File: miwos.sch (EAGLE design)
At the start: 44 parts

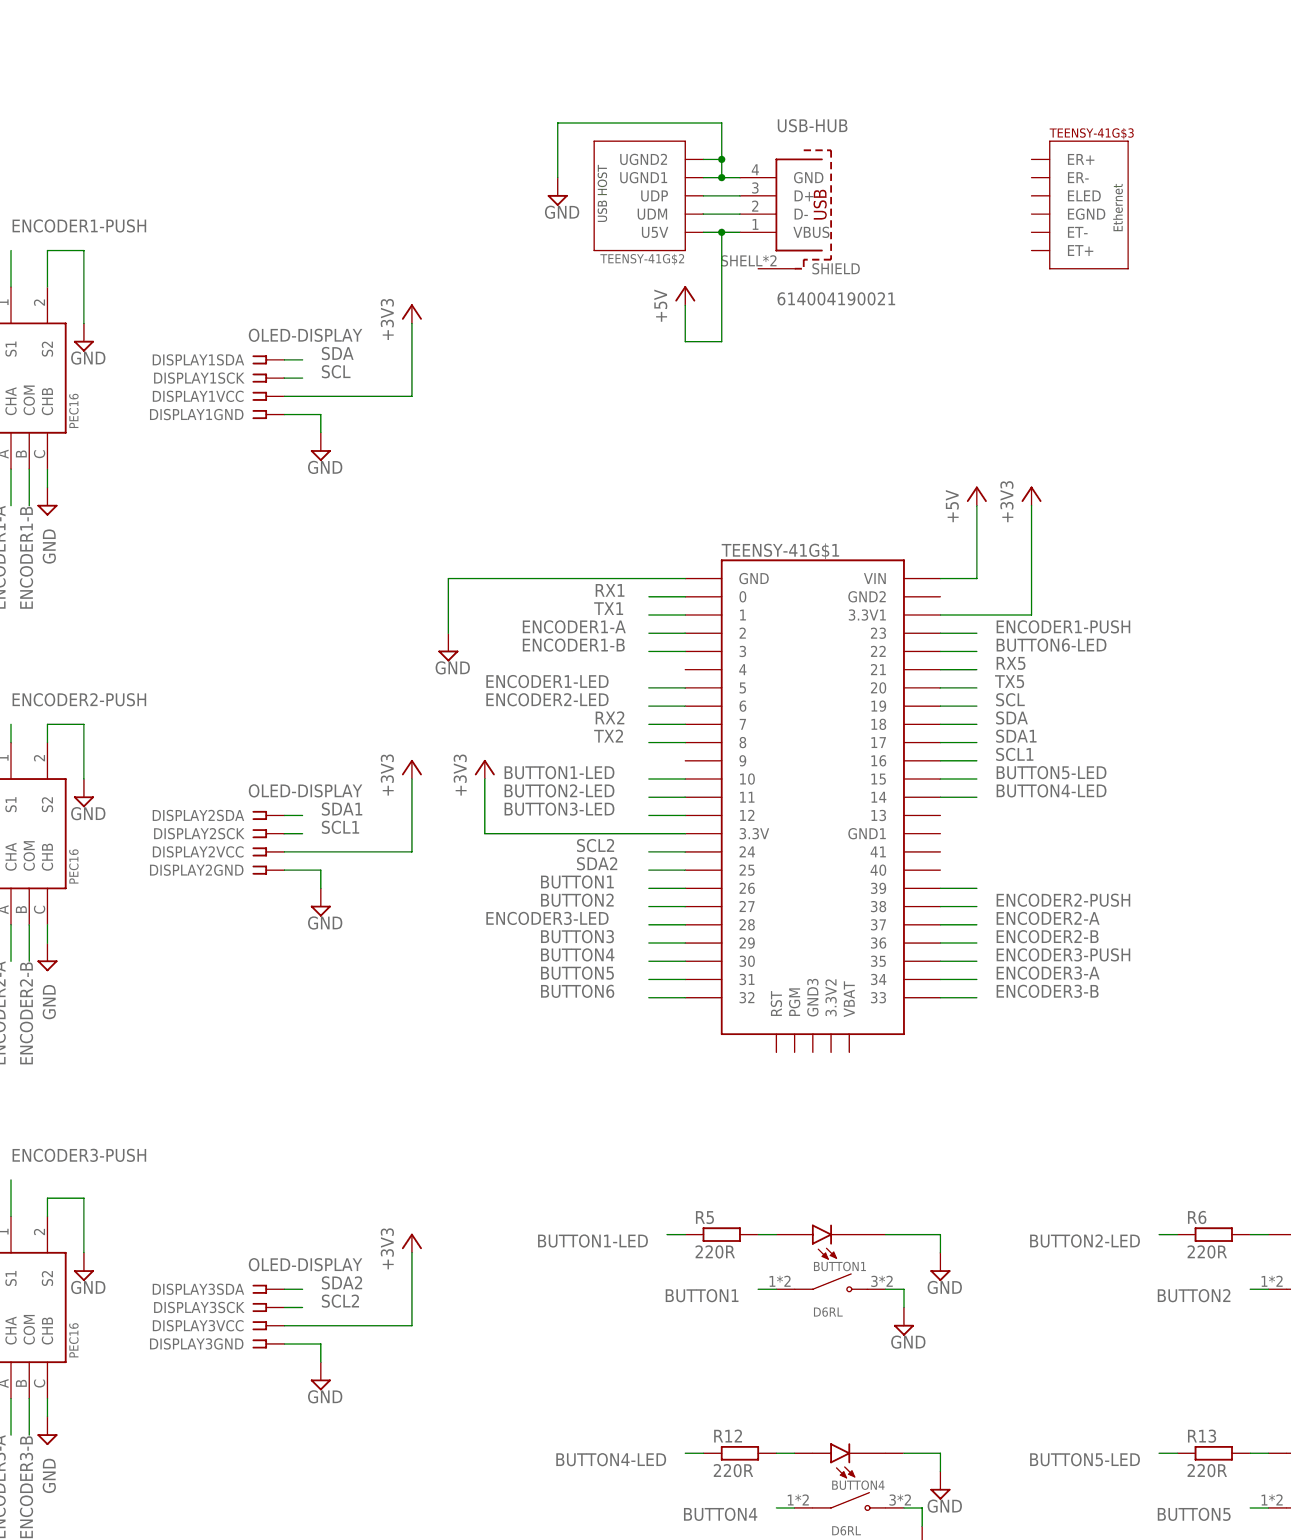
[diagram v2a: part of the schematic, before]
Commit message: Use DFR0647 displays
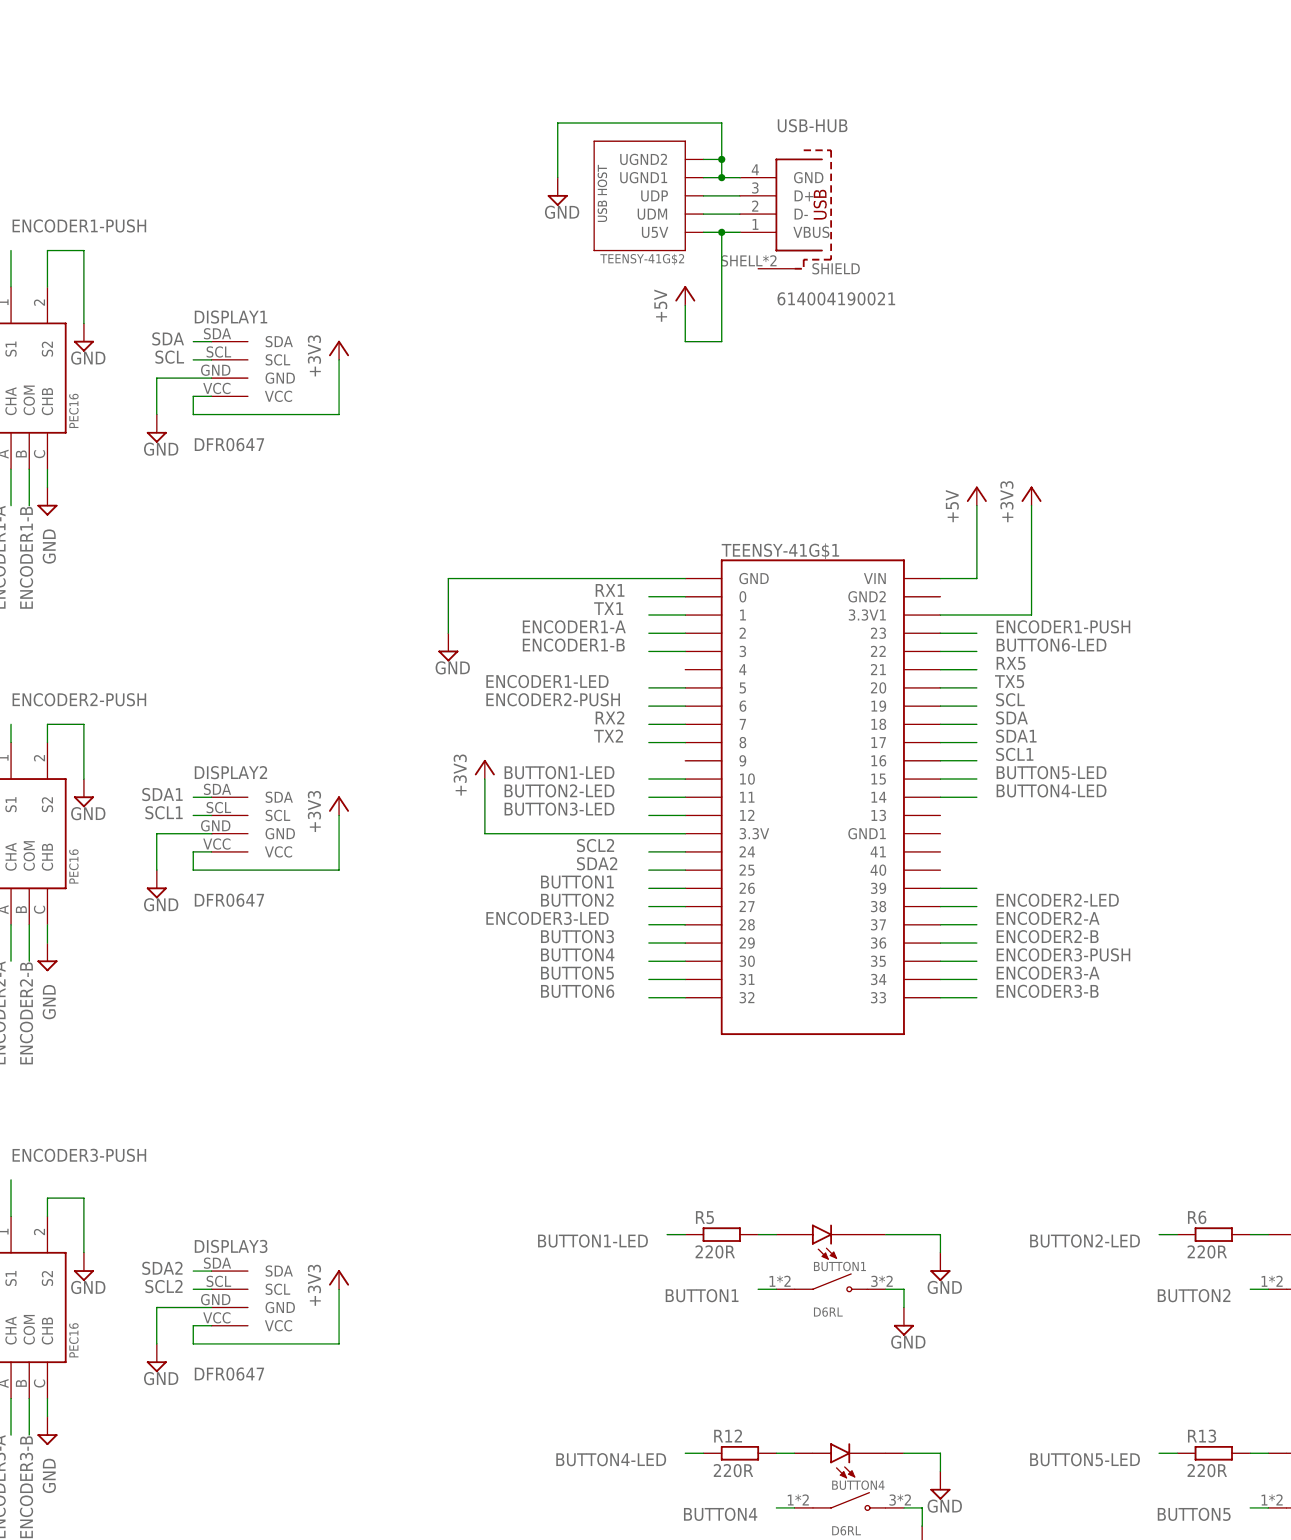
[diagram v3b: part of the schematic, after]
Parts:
- DISPLAY1, DISPLAY2, DISPLAY3: value OLED-DISPLAY -> DFR0647; device oled-display:OLED-DISPLAY -> DFR0647:DFR0647
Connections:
- net +3V3: now also DISPLAY1.VCC, DISPLAY2.VCC, DISPLAY3.VCC; no longer DISPLAY1VCC.1, DISPLAY2VCC.1, DISPLAY3VCC.1
- net ENCODER2-LED: now also TEENSY-41G$1.38; no longer TEENSY-41G$1.6
- net ENCODER2-PUSH: now also TEENSY-41G$1.6; no longer TEENSY-41G$1.38
- net GND: now also DISPLAY1.GND, DISPLAY2.GND, DISPLAY3.GND; no longer DISPLAY1GND.1, DISPLAY2GND.1, DISPLAY3GND.1
- net SCL: now also DISPLAY1.SCL; no longer DISPLAY1SCK.1
- net SCL1: now also DISPLAY2.SCL; no longer DISPLAY2SCK.1
- net SCL2: now also DISPLAY3.SCL; no longer DISPLAY3SCK.1
- net SDA: now also DISPLAY1.SDA; no longer DISPLAY1SDA.1
- net SDA1: now also DISPLAY2.SDA; no longer DISPLAY2SDA.1
- net SDA2: now also DISPLAY3.SDA; no longer DISPLAY3SDA.1

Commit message: Use 6N138 SMD footprint
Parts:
- OK1, OK2: device optocoupler:6N138 -> 6N138:6N138
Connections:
- net ENCODER1-B: now also ENCODER1.CHB; no longer ENCODER1.COM
- net ENCODER2-B: now also ENCODER2.CHB; no longer ENCODER2.COM
- net ENCODER3-B: now also ENCODER3.CHB; no longer ENCODER3.COM
- net GND: now also ENCODER1.COM, ENCODER2.COM, ENCODER3.COM; no longer ENCODER1.CHB, ENCODER2.CHB, ENCODER3.CHB
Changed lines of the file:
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@@
 <part name="SUPPLY5" library="supply2" library_urn="urn:adsk.eagle:library:372" deviceset="GND" device=""/>
 <part name="SUPPLY6" library="supply2" library_urn="urn:adsk.eagle:library:372" deviceset="GND" device=""/>
-<part name="OK1" library="optocoupler" library_urn="urn:adsk.eagle:library:320" deviceset="6N138" device="" package3d_urn="urn:adsk.eagle:package:21941/1"/>
+<part name="OK1" library="6N138" deviceset="6N138" device="" package3d_urn="urn:adsk.eagle:package:21941/1"/>
 <part name="MIDI2-IN" library="adafruit-5pin-din" deviceset="ADAFRUIT-5PIN-DIN" device=""/>
 <part name="SUPPLY7" library="supply2" library_urn="urn:adsk.eagle:library:372" deviceset="GND" device=""/>
@@
 <part name="SUPPLY19" library="supply2" library_urn="urn:adsk.eagle:library:372" deviceset="GND" device=""/>
 <part name="R7" library="rcl" library_urn="urn:adsk.eagle:library:334" deviceset="R-EU_" device="R0603" package3d_urn="urn:adsk.eagle:package:23555/3" value="220R"/>
-<part name="OK2" library="optocoupler" library_urn="urn:adsk.eagle:library:320" deviceset="6N138" device="" package3d_urn="urn:adsk.eagle:package:21941/1"/>
+<part name="OK2" library="6N138" deviceset="6N138" device="" package3d_urn="urn:adsk.eagle:package:21941/1"/>
 <part name="MIDI1-IN" library="adafruit-5pin-din" deviceset="ADAFRUIT-5PIN-DIN" device=""/>
 <part name="SUPPLY20" library="supply2" library_urn="urn:adsk.eagle:library:372" deviceset="GND" device=""/>
@@
 </segment>
 <segment>
-<pinref part="ENCODER1" gate="G$1" pin="CHB"/>
+<pinref part="ENCODER1" gate="G$1" pin="COM"/>
 <pinref part="SUPPLY1" gate="GND" pin="GND"/>
 <wire x1="-81.28" y1="104.14" x2="-81.28" y2="106.68" width="0.1524" layer="91"/>
 </segment>
 <segment>
-<pinref part="ENCODER2" gate="G$1" pin="CHB"/>
+<pinref part="ENCODER2" gate="G$1" pin="COM"/>
 <pinref part="SUPPLY3" gate="GND" pin="GND"/>
 <wire x1="-81.28" y1="43.18" x2="-81.28" y2="40.64" width="0.1524" layer="91"/>
 </segment>
 <segment>
-<pinref part="ENCODER3" gate="G$1" pin="CHB"/>
+<pinref part="ENCODER3" gate="G$1" pin="COM"/>
 <wire x1="-81.28" y1="-22.86" x2="-81.28" y2="-25.4" width="0.1524" layer="91"/>
 <pinref part="SUPPLY5" gate="GND" pin="GND"/>
@@
 </segment>
 <segment>
-<pinref part="ENCODER3" gate="G$1" pin="COM"/>
+<pinref part="ENCODER3" gate="G$1" pin="CHB"/>
 <wire x1="-83.82" y1="-22.86" x2="-83.82" y2="-27.94" width="0.1524" layer="91"/>
 <label x="-85.09" y="-27.94" size="1.778" layer="95" rot="R270"/>
@@
 </segment>
 <segment>
-<pinref part="ENCODER2" gate="G$1" pin="COM"/>
+<pinref part="ENCODER2" gate="G$1" pin="CHB"/>
 <wire x1="-83.82" y1="43.18" x2="-83.82" y2="38.1" width="0.1524" layer="91"/>
 <label x="-85.09" y="38.1" size="1.778" layer="95" rot="R270"/>
@@
 </segment>
 <segment>
-<pinref part="ENCODER1" gate="G$1" pin="COM"/>
+<pinref part="ENCODER1" gate="G$1" pin="CHB"/>
 <wire x1="-83.82" y1="106.68" x2="-83.82" y2="101.6" width="0.1524" layer="91"/>
 <label x="-85.09" y="101.6" size="1.778" layer="95" rot="R270"/>

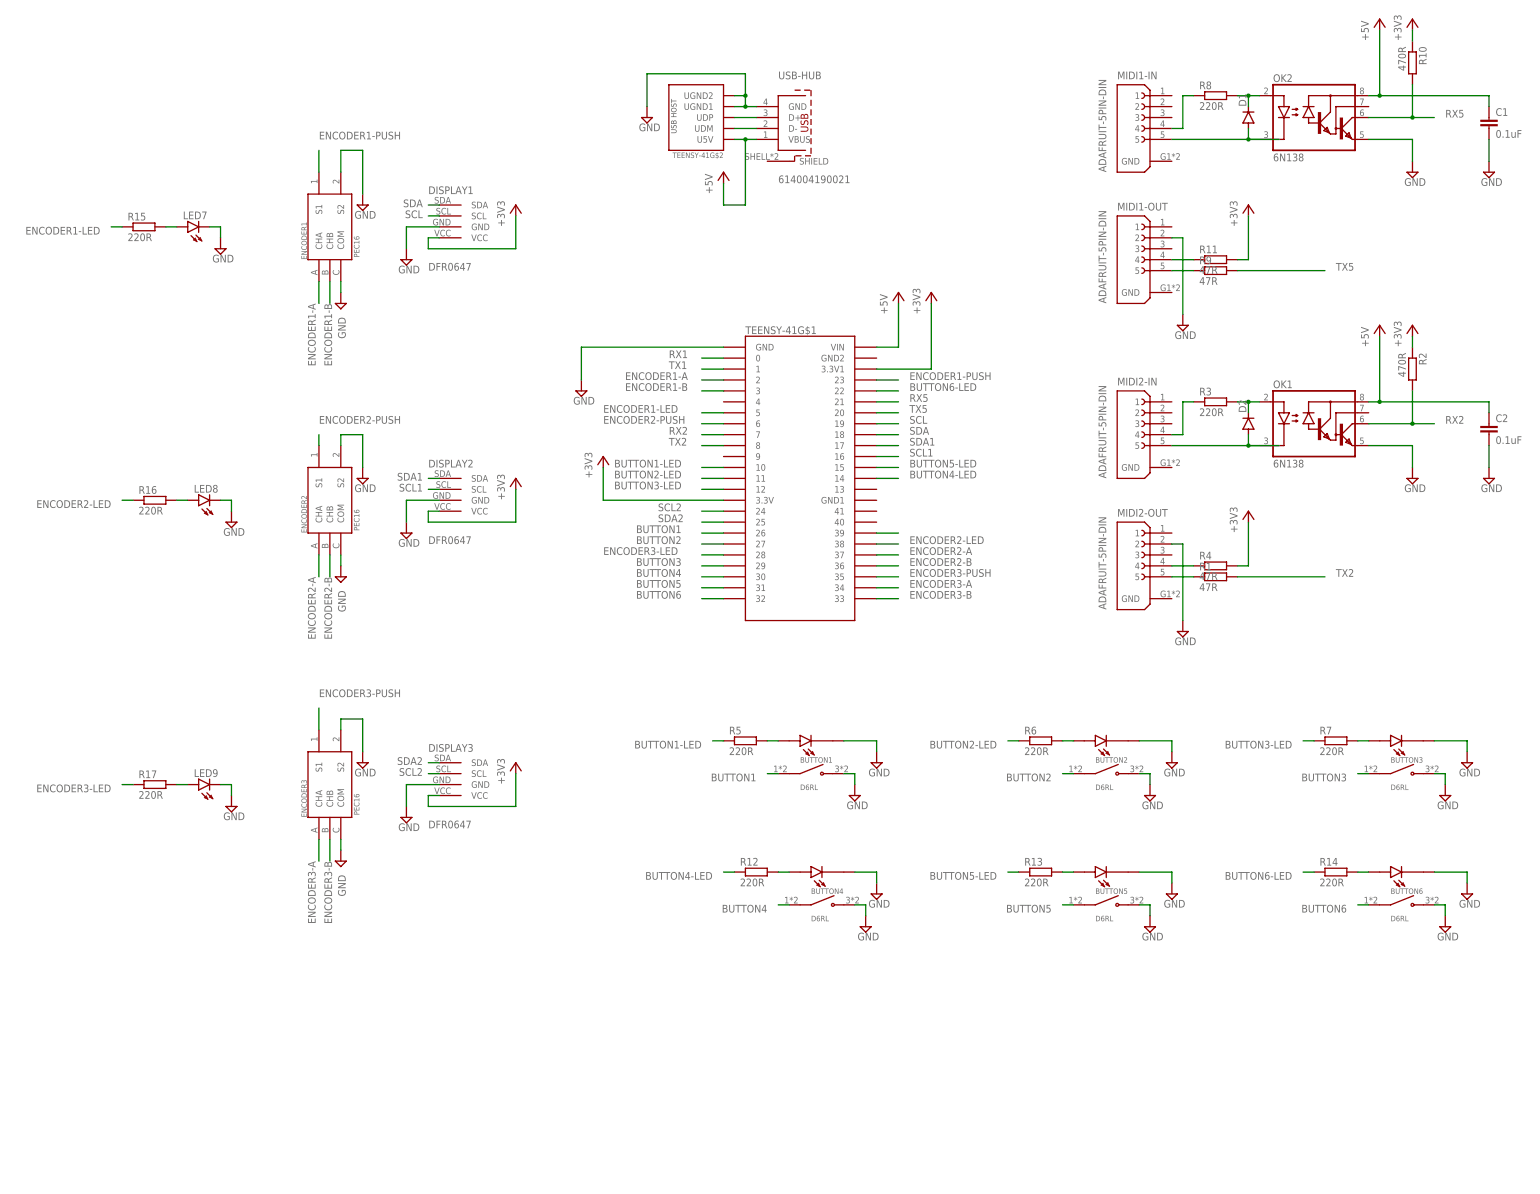
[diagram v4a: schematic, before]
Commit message: Add shift/menu button
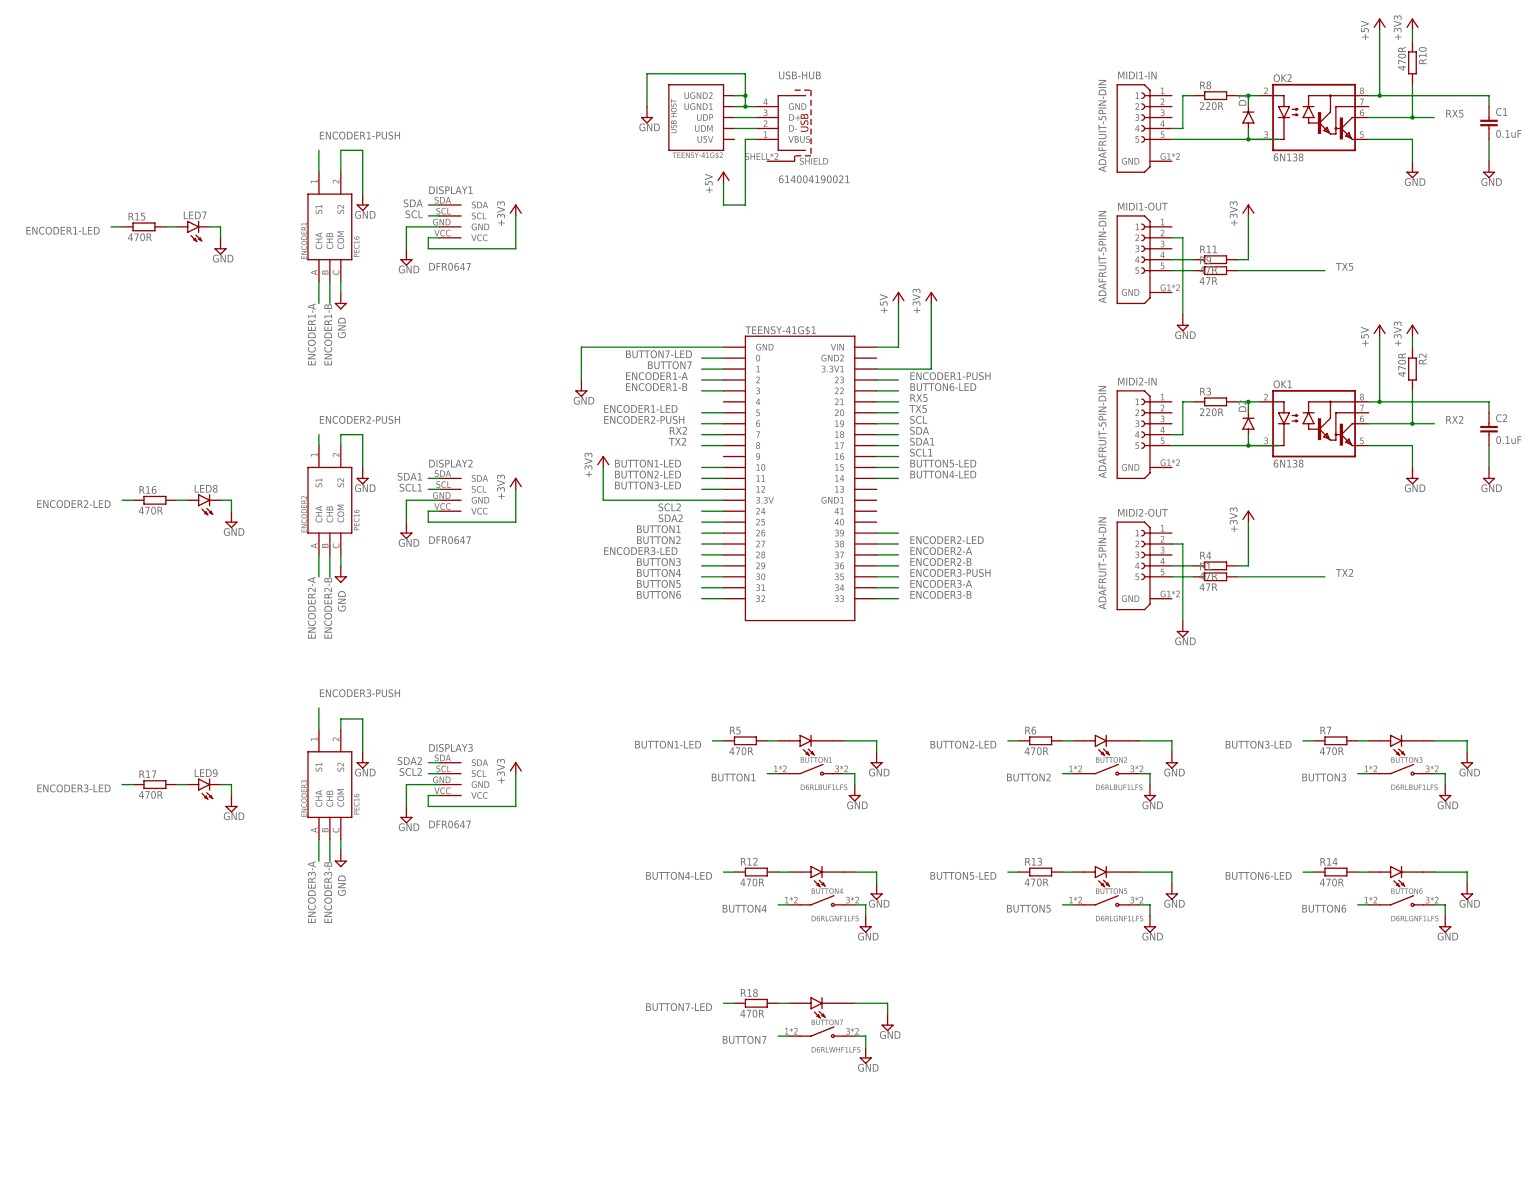
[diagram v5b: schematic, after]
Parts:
- added BUTTON7: D6RLWHF1LFS, D6RL:D6RLWHF1LFS
- added R18: 470R, rcl:R-EU_R0603
- BUTTON1, BUTTON2, BUTTON3: value D6RL -> D6RLBUF1LFS; device D6RL:D6RL -> D6RL:D6RLBUF1LFS
- BUTTON4, BUTTON5, BUTTON6: value D6RL -> D6RLGNF1LFS; device D6RL:D6RL -> D6RL:D6RLGNF1LFS
- R12, R13, R14, R15, R16, R17, R5, R6, R7: value 220R -> 470R
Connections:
- removed net RX1: TEENSY-41G$1.0
- removed net TX1: TEENSY-41G$1.1
- new net BUTTON7: BUTTON7.COM, TEENSY-41G$1.1
- new net BUTTON7-LED: R18.1, TEENSY-41G$1.0
- new net N$7: BUTTON7.LED, R18.2
- net +5V: no longer TEENSY-41G$2.U5V
- net GND: now also BUTTON7.COM-LED, BUTTON7.NO
